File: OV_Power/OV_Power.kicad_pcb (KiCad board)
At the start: 4 copper layers, 90 x 60 mm, 78 parts, among them CN1 CONN_HEADER_R_A_2POS_2.5MM, J1 Kycon_kpjx-4s, J2 Conn_HDR_2x10_latching, J3 532530670, J4 SpadeLug, J5 SpadeLug, J6 CONN_HEADER_2.54X2_MOLEX_KK_S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, J7 CONN_HEADER_2.54X2_MOLEX_KK_S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, Q1 SSM3K341R, Q2 2N7002BK, Q3 SZNUD3124LT1G, Q4 SZNUD3124LT1G, U1 LT3796, U2 LT1936, U3 LT6106, U4 VNH5019ATR-E, U7 LTC4416, U8 AOSD21307, U9 AOSD21307

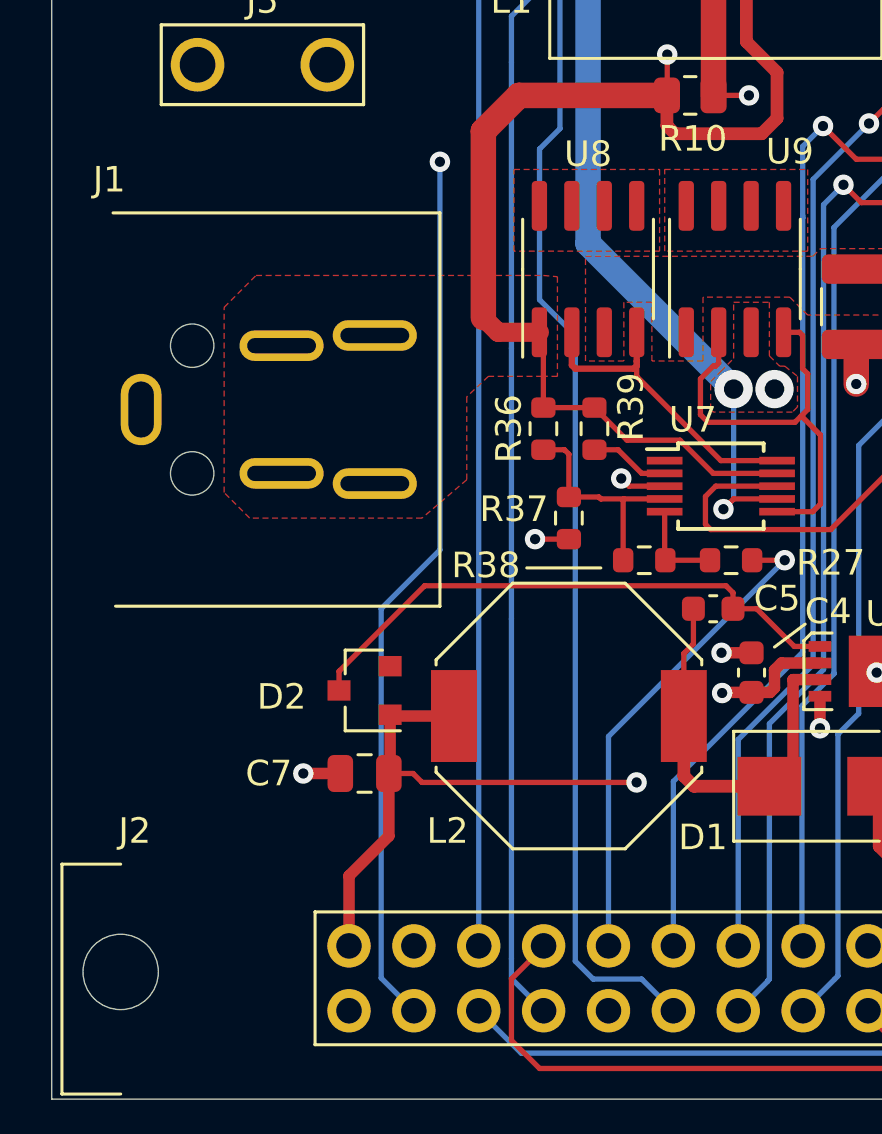
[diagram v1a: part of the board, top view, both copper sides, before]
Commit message: Changed the power input jack to a shielded version of the same part. Note that the same footprint can be used with either shielded or unshielded versions.
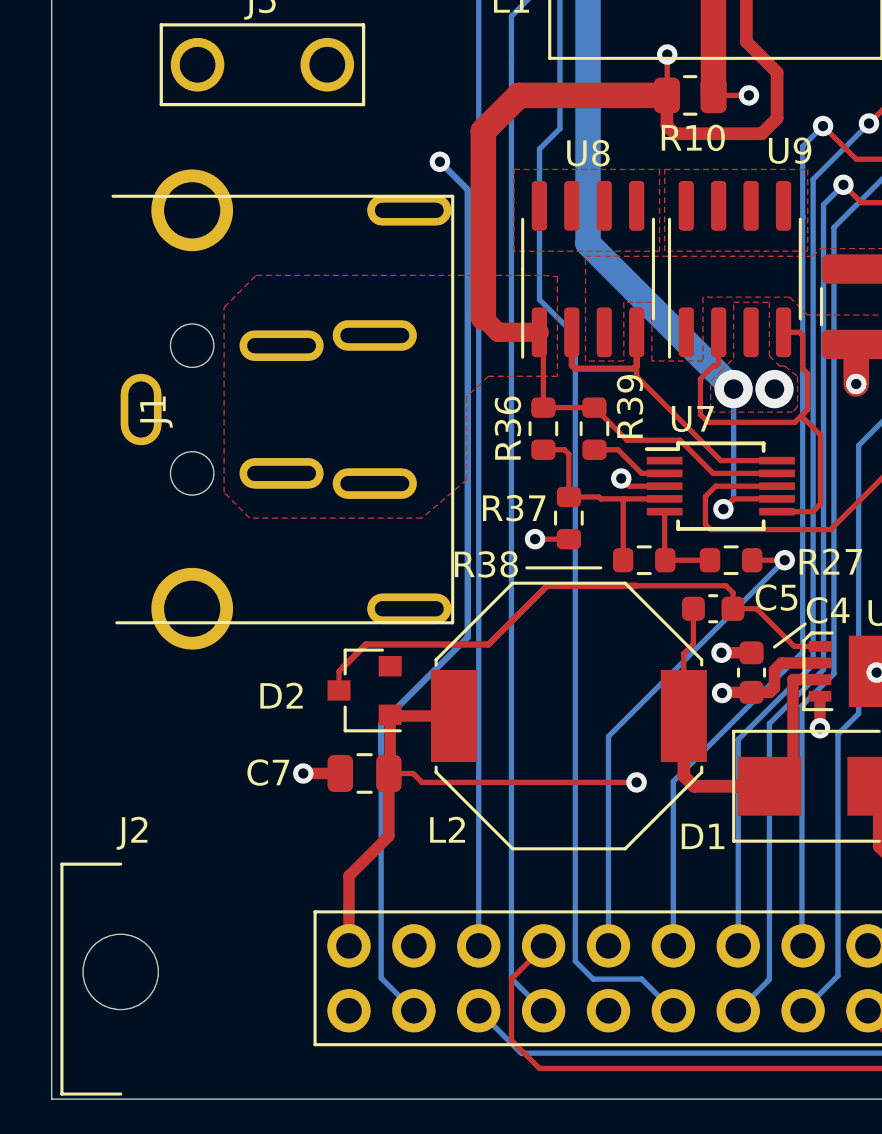
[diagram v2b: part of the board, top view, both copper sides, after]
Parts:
- J1: value Kycon_kpjx-4s -> Kycon_kpjx-4s_shielded; footprint OpenVent:Kycon_KPJX-4S -> OpenVent:Kycon_KPJX-4S_SHIELD
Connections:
- J1 pad 5: (no net) -> GND
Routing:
- net CHG_CURRENT: track 88.3 -> 89.2 mm

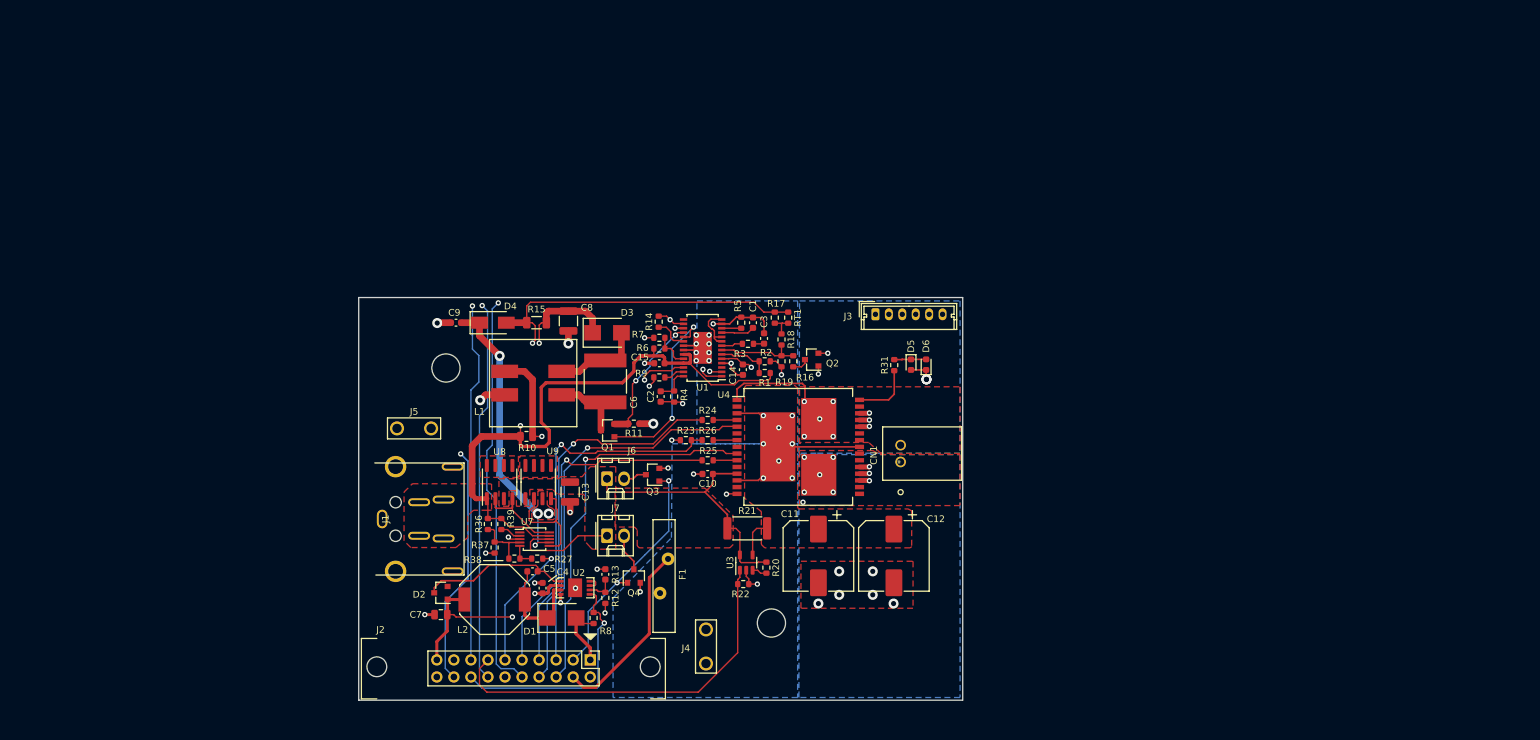
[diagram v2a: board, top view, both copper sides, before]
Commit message: Re-jigging the pcb outline for the power board...
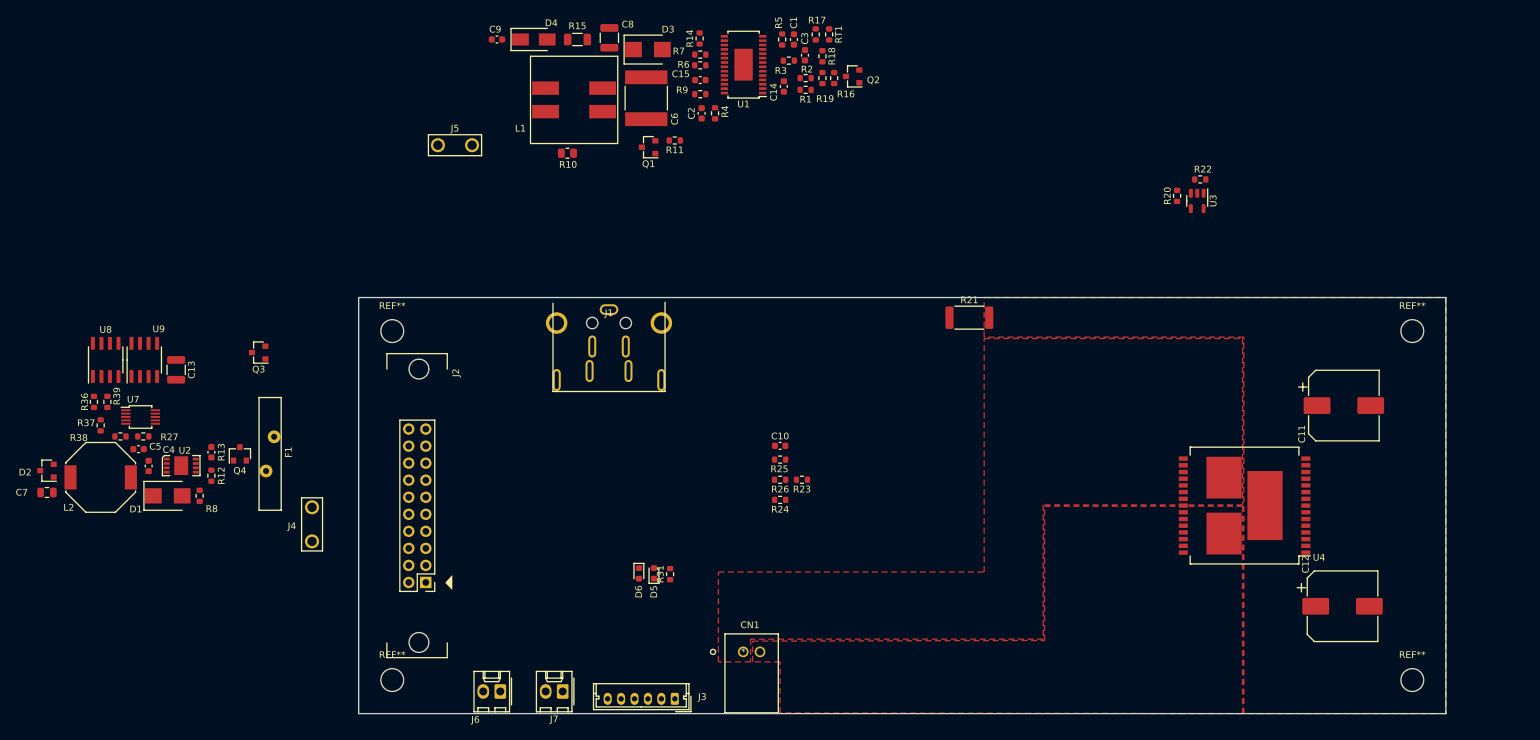
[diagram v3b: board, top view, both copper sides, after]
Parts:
- removed the REF** at (91.5, 78.5)
- removed the REF** at (43.0, 40.5)
- added REF**: MountingHole_3.4mm_M3, OpenVent:MountingHole_3.4mm_M3, F.Cu at (187.0, 87.0)
- added REF**: MountingHole_3.4mm_M3, OpenVent:MountingHole_3.4mm_M3, F.Cu at (187.0, 35.0)
- added REF**: MountingHole_3.4mm_M3, OpenVent:MountingHole_3.4mm_M3, F.Cu at (35.0, 35.0)
- added REF**: MountingHole_3.4mm_M3, OpenVent:MountingHole_3.4mm_M3, F.Cu at (35.0, 87.0)
- moved R22 91.0 mm to (155.4, 12.4), turned to 180 degrees
- moved U3 86.1 mm to (154.9, 15.6), turned to 270 degrees
- moved R20 82.6 mm to (151.9, 14.8), turned to 90 degrees
- moved C11 81.4 mm to (176.8, 46.1), turned to 0 degrees
- moved C12 67.3 mm to (176.6, 76.0), turned to 0 degrees
- moved U4 67.1 mm to (162.0, 61.0), turned to 180 degrees
- moved J3 64.6 mm to (77.1, 89.8), turned to 180 degrees
- moved C13 61.5 mm to (2.80, 40.8)
- moved C7 61.5 mm to (-16.4, 59.0)
- moved D1 61.5 mm to (1.55, 59.5)
- moved D2 61.5 mm to (-16.4, 55.8)
- moved F1 61.5 mm to (16.8, 53.3)
- moved J4 61.5 mm to (23.1, 63.8)
- moved L2 61.5 mm to (-8.45, 56.8)
- moved Q4 61.5 mm to (12.3, 53.3)
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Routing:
- net Net-(J2-Pad15): track 121.8 -> 0.00 mm, vias 1 -> 0
- net Net-(J2-Pad14): track 120.9 -> 0.00 mm, vias 1 -> 0
- net Net-(J2-Pad10): track 117.0 -> 0.00 mm, vias 1 -> 0
- net VIN_12V: track 116.5 -> 0.00 mm, vias 2 -> 0
- net V_MAIN: track 96.0 -> 0.00 mm, vias 1 -> 0
- net CHG_CURRENT: track 89.2 -> 0.00 mm, vias 2 -> 0
- net Net-(D4-Pad2): track 79.9 -> 0.00 mm, vias 2 -> 0
- net GND: track 78.6 -> 0.00 mm, vias 45 -> 0
- net VBATT: track 69.5 -> 0.00 mm, vias 4 -> 0
- net V7.5V: track 68.0 -> 0.00 mm, vias 2 -> 0
- net MOTOR_CURRENT: track 58.0 -> 0.00 mm
- net nMOTOR-FAULT-B: track 57.6 -> 0.00 mm, vias 1 -> 0
- net PWM: track 57.5 -> 0.00 mm, vias 1 -> 0
- net nMOTOR-FAULT-A: track 57.2 -> 0.00 mm, vias 1 -> 0
- net MOTOR-IN-A: track 55.5 -> 0.00 mm, vias 1 -> 0
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- removed copper zone on F.Cu, net GND
- removed copper zone on B.Cu, net Net-(C11-Pad1)
- removed copper zone on B.Cu, net Net-(CN1-Pad1)
- removed copper zone on B.Cu, net Net-(CN1-Pad2)
- removed copper zone on In2.Cu, net Net-(F1-Pad1)
- removed copper zone on F.Cu, net Net-(U8-Pad5)
- removed copper zone on F.Cu, net Net-(U9-Pad5)
- removed copper zone on F.Cu, net VBATT
- removed copper zone on In2.Cu, net VBATT
- removed copper zone on F.Cu, net VIN_12V
- removed copper zone on F.Cu, net V_MAIN
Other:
- board size 90 x 60 mm -> 162 x 62 mm

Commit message: Tentative placement (again...) for power board, also added a ferrite part for Shrouk to the main library.
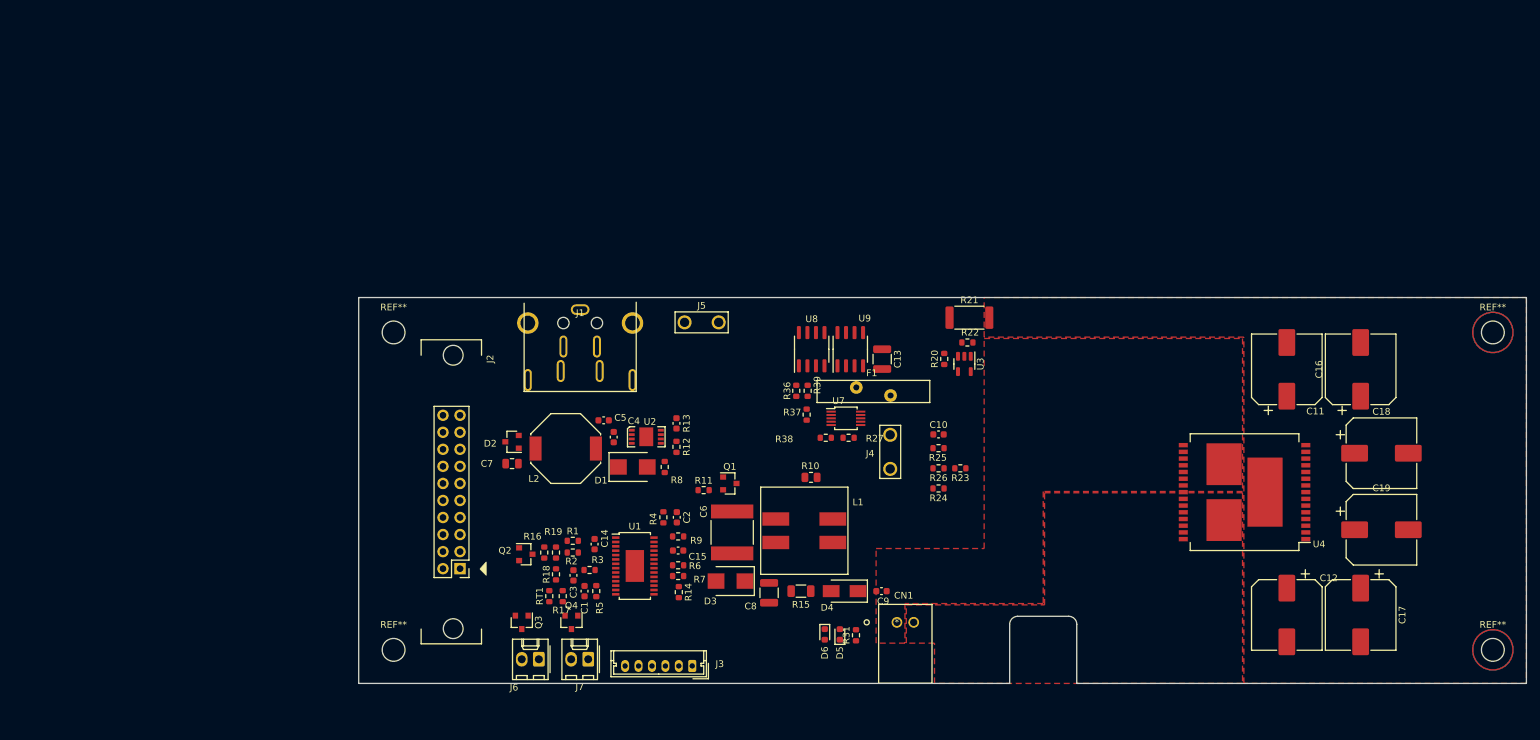
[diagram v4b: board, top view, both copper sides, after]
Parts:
- added C16: 1000uF_25V_Aluminium_SMD_Capacitor,_20%, Capacitor_SMD:CP_Elec_10x10, F.Cu at (179.3, 40.7)
- added C17: 1000uF_25V_Aluminium_SMD_Capacitor,_20%, Capacitor_SMD:CP_Elec_10x10, F.Cu at (179.3, 77.3)
- added C18: 1000uF_25V_Aluminium_SMD_Capacitor,_20%, Capacitor_SMD:CP_Elec_10x10, F.Cu at (182.4, 53.2)
- added C19: 1000uF_25V_Aluminium_SMD_Capacitor,_20%, Capacitor_SMD:CP_Elec_10x10, F.Cu at (182.4, 64.6)
- moved C13 105.2 mm to (108.0, 39.2)
- moved R37 105.2 mm to (96.8, 47.5)
- moved U8 105.2 mm to (97.5, 37.7)
- moved U9 105.2 mm to (103.2, 37.7)
- moved R27 105.1 mm to (103.0, 50.9)
- moved R38 105.1 mm to (99.6, 50.9)
- moved U7 105.1 mm to (102.6, 48.0)
- moved R36 104.7 mm to (95.2, 43.9)
- moved R39 104.4 mm to (96.9, 43.9)
- moved C9 100.2 mm to (107.9, 73.8), turned to 0 degrees
- moved D4 94.3 mm to (102.4, 73.8), turned to 180 degrees
- moved RT1 93.5 mm to (58.4, 74.5), turned to 90 degrees
- moved R17 91.8 mm to (60.4, 74.5), turned to 90 degrees
- moved F1 90.4 mm to (106.7, 44.0), turned to 180 degrees
- moved R15 88.7 mm to (95.9, 73.8), turned to 0 degrees
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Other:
- board size 162 x 62 mm -> 174 x 57.5 mm

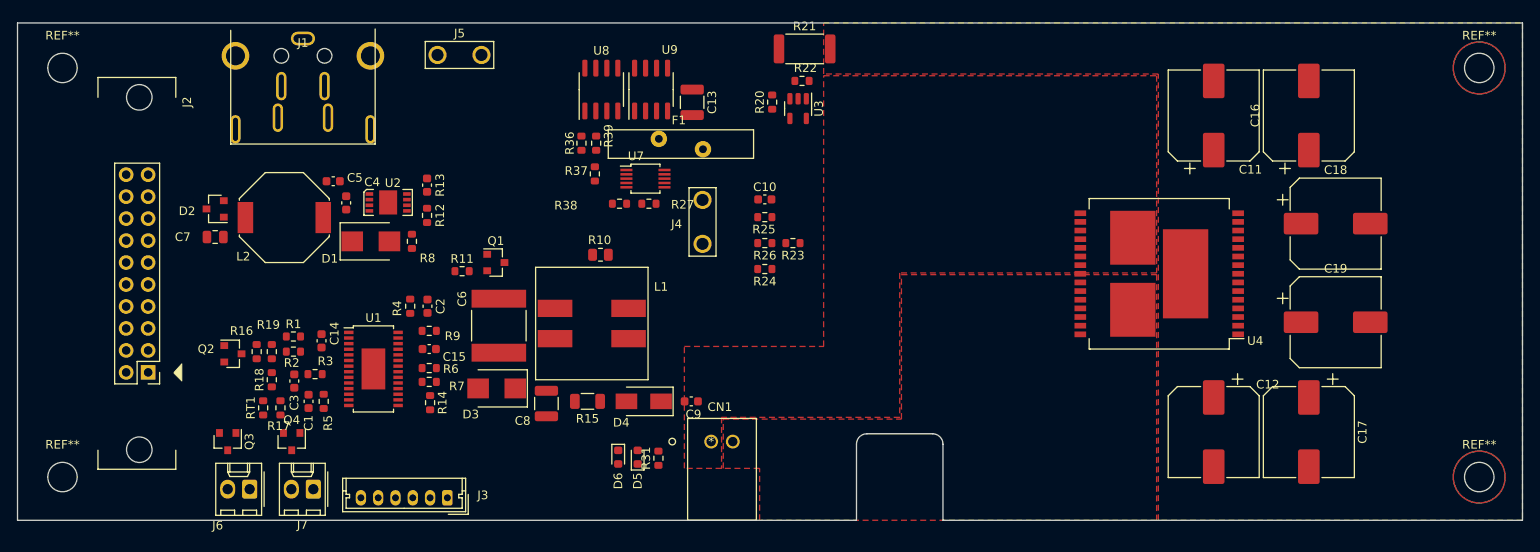
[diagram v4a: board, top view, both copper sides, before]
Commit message: Finally getting on with board routing, in TWO layers.  Warning, some things changed on the 20 pin interconnect.
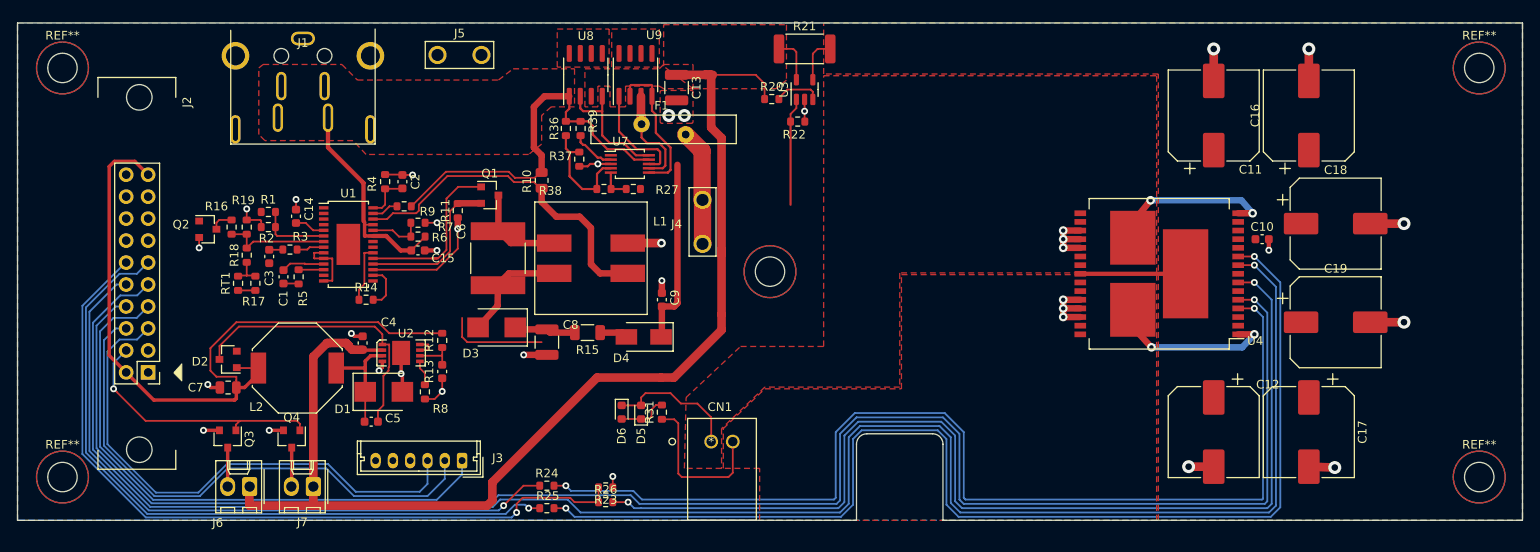
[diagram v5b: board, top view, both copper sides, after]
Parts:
- added REF**: MountingHole_3.4mm_M3, OpenVent:MountingHole_3.4mm_M3, F.Cu at (117.0, 58.8)
- moved C10 57.7 mm to (173.9, 55.0)
- moved R25 42.0 mm to (91.2, 86.1), turned to 0 degrees
- moved R23 35.6 mm to (98.0, 83.7)
- moved R24 35.5 mm to (91.2, 83.5), turned to 0 degrees
- moved R26 35.2 mm to (98.0, 85.4), turned to 0 degrees
- moved C5 28.1 mm to (70.9, 76.1)
- moved R13 21.6 mm to (79.1, 70.3), turned to 270 degrees
- moved R7 18.4 mm to (76.3, 53.1)
- moved C7 17.5 mm to (54.4, 72.2)
- moved D1 17.5 mm to (72.3, 72.7)
- moved D2 17.5 mm to (54.4, 68.9)
- moved L2 17.5 mm to (62.4, 69.9)
- moved R8 17.5 mm to (77.1, 72.7)
- moved U2 17.5 mm to (74.3, 68.2)
- moved C4 16.3 mm to (69.9, 67.0)
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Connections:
- C10 pad 1: V_MAIN -> Net-(C10-Pad1)
- C11 pad 1: Net-(C11-Pad1) -> Net-(C10-Pad1)
- C12 pad 1: Net-(C11-Pad1) -> Net-(C10-Pad1)
- C16 pad 1: Net-(C11-Pad1) -> Net-(C10-Pad1)
- C17 pad 1: Net-(C11-Pad1) -> Net-(C10-Pad1)
- C18 pad 1: Net-(C11-Pad1) -> Net-(C10-Pad1)
- C19 pad 1: Net-(C11-Pad1) -> Net-(C10-Pad1)
- J2 pad 10: Net-(J2-Pad10) -> MOTOR-IN-A
- J2 pad 11: /Power Supply/POWER_STATUS -> MOTOR-IN-B
- J2 pad 12: Net-(J2-Pad12) -> PWM
- J2 pad 15: Net-(J2-Pad15) -> /Power Supply/POWER_STATUS
- J2 pad 3: /Power Supply/FAN_DRIVE -> VBATT
- J2 pad 4: VBATT -> /Power Supply/FAN_DRIVE
- J2 pad 5: nMOTOR-FAULT-A -> Net-(J2-Pad5)
- J2 pad 6: nMOTOR-FAULT-B -> Net-(J2-Pad6)
- J2 pad 7: MOTOR-IN-A -> Net-(J2-Pad7)
- J2 pad 8: MOTOR-IN-B -> nMOTOR-FAULT-A
- J2 pad 9: PWM -> nMOTOR-FAULT-B
- J3 pad 1: Net-(J2-Pad10) -> Net-(J2-Pad7)
- J3 pad 2: Net-(J2-Pad14) -> Net-(J2-Pad6)
- J3 pad 3: Net-(J2-Pad15) -> Net-(J2-Pad5)
- R21 pad 2: Net-(C11-Pad1) -> Net-(C10-Pad1)
- U3 pad 4: Net-(C11-Pad1) -> Net-(C10-Pad1)
- U4 pad 12: V_MAIN -> Net-(C10-Pad1)
- U4 pad 13: Net-(C11-Pad1) -> Net-(C10-Pad1)
- U4 pad 23: Net-(C11-Pad1) -> Net-(C10-Pad1)
- U4 pad 3: Net-(C11-Pad1) -> Net-(C10-Pad1)
- U4 pad 31: Net-(C11-Pad1) -> Net-(C10-Pad1)
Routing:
- net nMOTOR-FAULT-B: track 0.00 -> 211.7 mm, vias 0 -> 1
- net nMOTOR-FAULT-A: track 0.00 -> 200.5 mm, vias 0 -> 1
- net V_MAIN: track 0.00 -> 154.5 mm
- net Net-(R25-Pad2): track 0.00 -> 134.2 mm, vias 0 -> 2
- net Net-(R24-Pad2): track 0.00 -> 124.2 mm, vias 0 -> 2
- net Net-(R26-Pad2): track 0.00 -> 122.2 mm, vias 0 -> 2
- net GND: track 0.00 -> 99.3 mm, vias 0 -> 35
- net PWM: track 0.00 -> 90.4 mm, vias 0 -> 1
- net V7.5V: track 0.00 -> 87.5 mm
- net MOTOR-IN-B: track 0.00 -> 82.1 mm, vias 0 -> 1
- net MOTOR-IN-A: track 0.00 -> 77.7 mm, vias 0 -> 1
- net VIN_12V: track 0.00 -> 69.7 mm
- net Net-(J2-Pad7): track 0.00 -> 67.3 mm
- net Net-(J2-Pad6): track 0.00 -> 62.7 mm
- net Net-(J2-Pad5): track 0.00 -> 61.6 mm
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- added copper zone on B.Cu, net GND
- added copper zone on F.Cu, net GND
- added copper zone on F.Cu, net Net-(C10-Pad1)
- added copper zone on F.Cu, net Net-(U8-Pad5)
- added copper zone on F.Cu, net Net-(U9-Pad5)
- added copper zone on F.Cu, net VIN_12V
- added copper zone on F.Cu, net V_MAIN
- removed copper zone on In1.Cu, net GND
- removed copper zone on F.Cu, net Net-(C11-Pad1)
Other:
- copper layers 4 -> 2
